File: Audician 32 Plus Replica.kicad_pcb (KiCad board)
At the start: 2 copper layers, 158.4 x 80.7 mm, 190 parts, among them CN1 CD-ROM, CN2 Waveblaster, J1 Bus_ISA_16bit, J10 Conn_01x04, J11 Conn_01x04, J13 Conn_01x04, J2 Audio Out, J3 Line Input, J4 Microphone, J5 Gameport, J7 Conn_01x04, J8 Conn_01x04, J9 Conn_01x04, Q1 HT7251, Q2 MMBT3904, U1 QS1000, U10 74LS138, U2 QS1001A, U3 TDA1311AT, U4 TDA1517/N3, U5 TEA2025B, U6 YMF719E-S, U7 Mysterious Chip, U8 MK1420S, U9 93C66C, X1 24MHz, X2 33.8688MHz, X3 24.576MHz

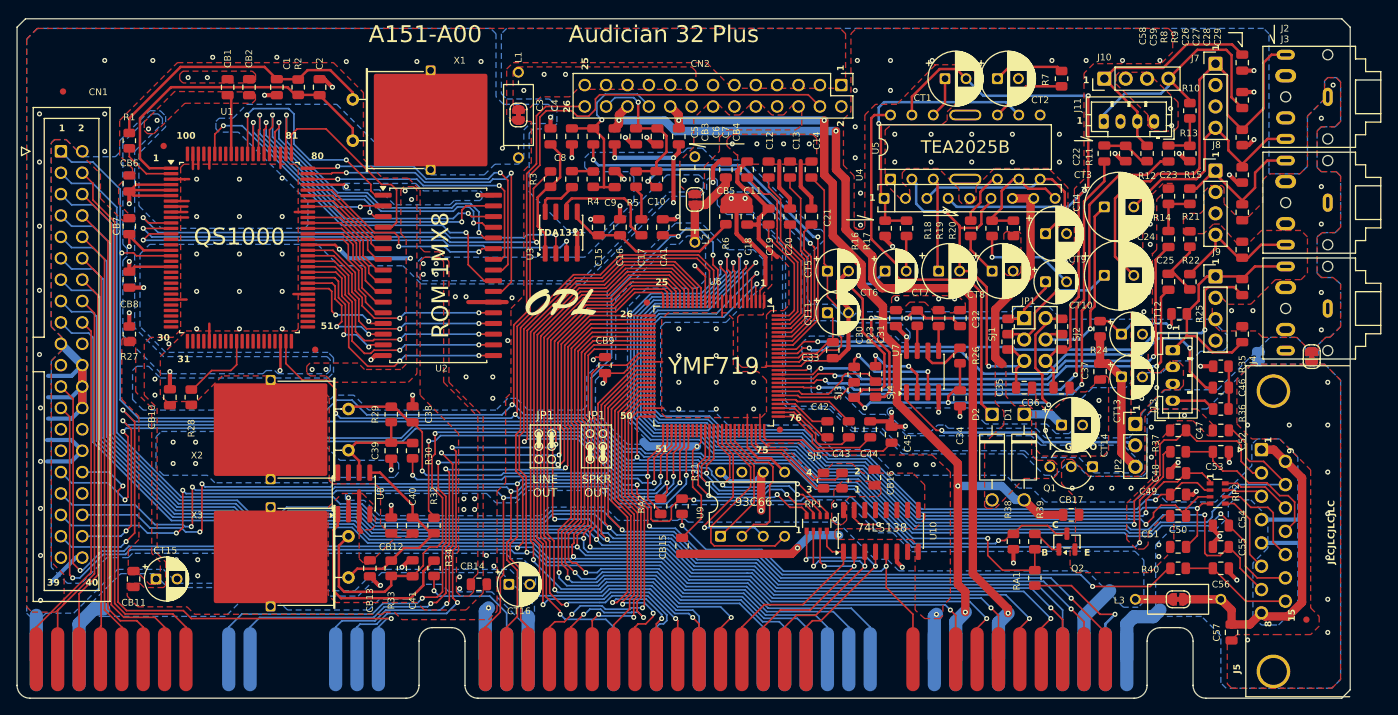
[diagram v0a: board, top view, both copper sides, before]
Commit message: Optimize routing
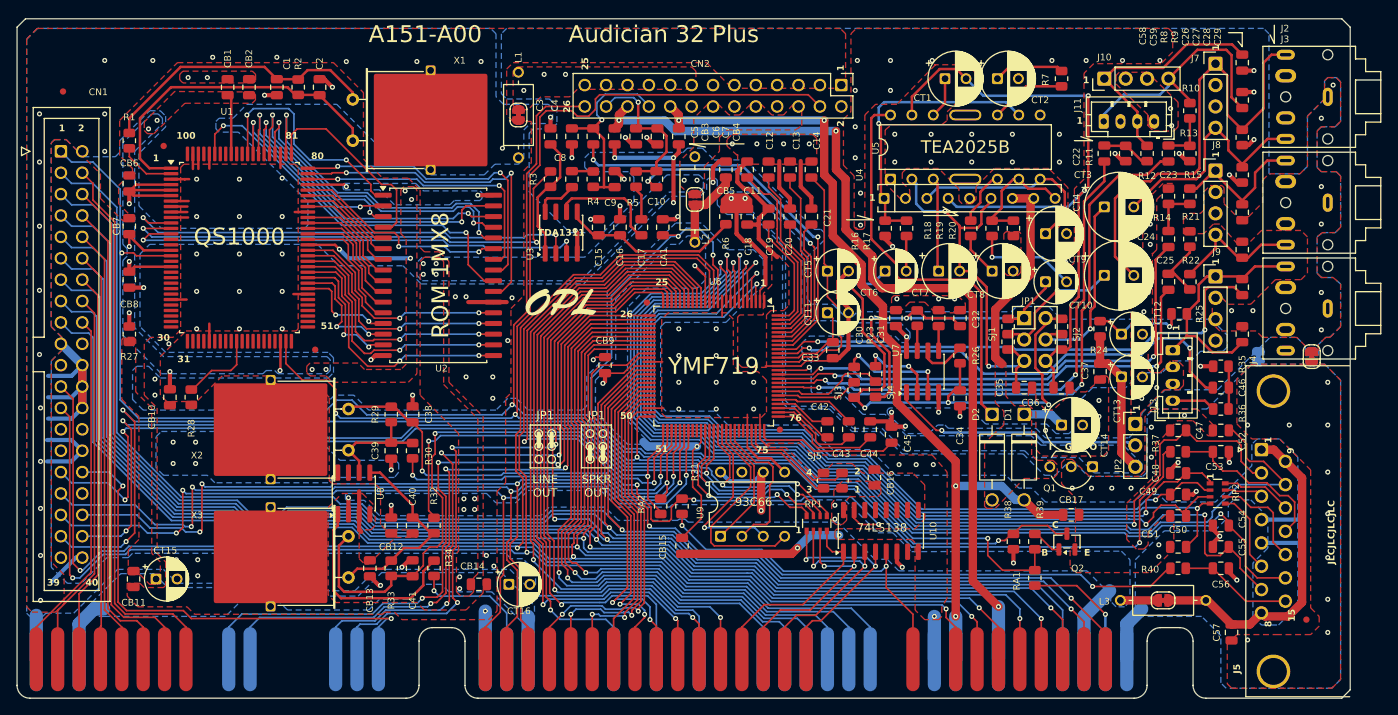
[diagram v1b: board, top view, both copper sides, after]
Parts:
- moved SJL3 1.78 mm to (205.6, 131.8)
- moved L3 1.78 mm to (200.6, 131.8)
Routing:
- net GND: track 193.6 -> 190.6 mm
- net D1: track 172.0 -> 170.1 mm
- net A11: track 85.5 -> 83.7 mm
- net A7: track 40.6 -> 39.0 mm
- net RESET: track 16.7 -> 15.1 mm
- net D4: track 178.8 -> 177.2 mm
- net IRQ5: track 73.4 -> 72.1 mm
- net A8: track 42.9 -> 41.8 mm
- net -12V: track 106.9 -> 105.9 mm
- net D3: track 179.3 -> 178.3 mm
- net A4: track 42.7 -> 41.8 mm
- net D2: track 174.2 -> 173.4 mm
- net +5VL: track 38.8 -> 39.5 mm
- net +12V: track 105.7 -> 105.0 mm
